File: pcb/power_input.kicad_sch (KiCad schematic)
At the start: 16 parts, among them K1 G4A-1A-E DC12, Q1 AO3400A

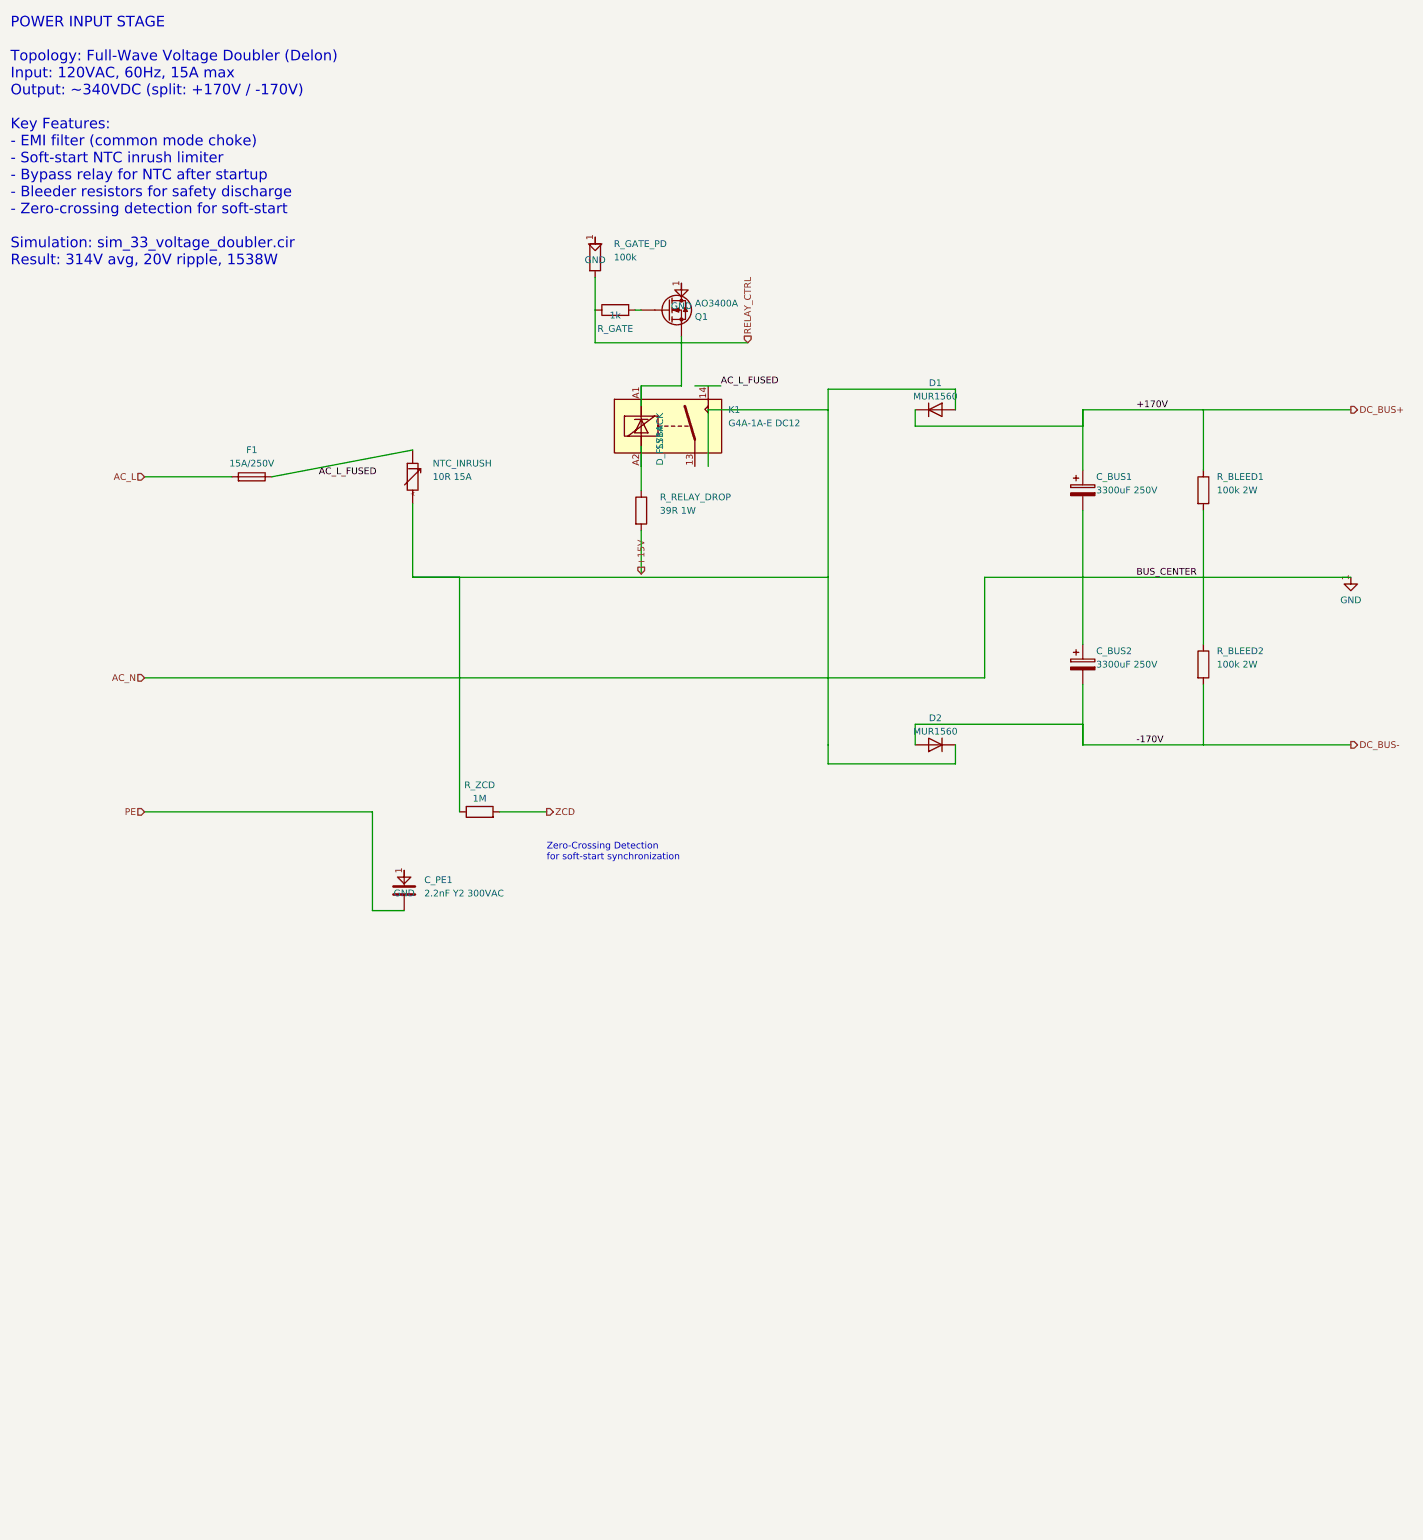
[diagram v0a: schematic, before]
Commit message: feat: generate KiCad schematics from atopile netlist
scripts/gen_schematics.py generates all 7 hierarchical KiCad schematic
files (root + 6 sub-sheets) from elec/build/default.net:

- Synthesizes box symbols from netlist libpart pin counts
- Pure label-per-pin connectivity (no wires)
- Hierarchical labels for inter-sheet nets
- Deterministic UUIDs from atopile tstamps
- Built-in oracle verifies connectivity partition isomorphism
- No-connect markers on intentionally-unconnected pins

Oracle: ORACLE PASS — 346 pin assignments, 73 multi-node nets,
connectivity partitions isomorphic.

Integrated into Makefile via 'make schematics' target.
Manifest entry added per repo convention.
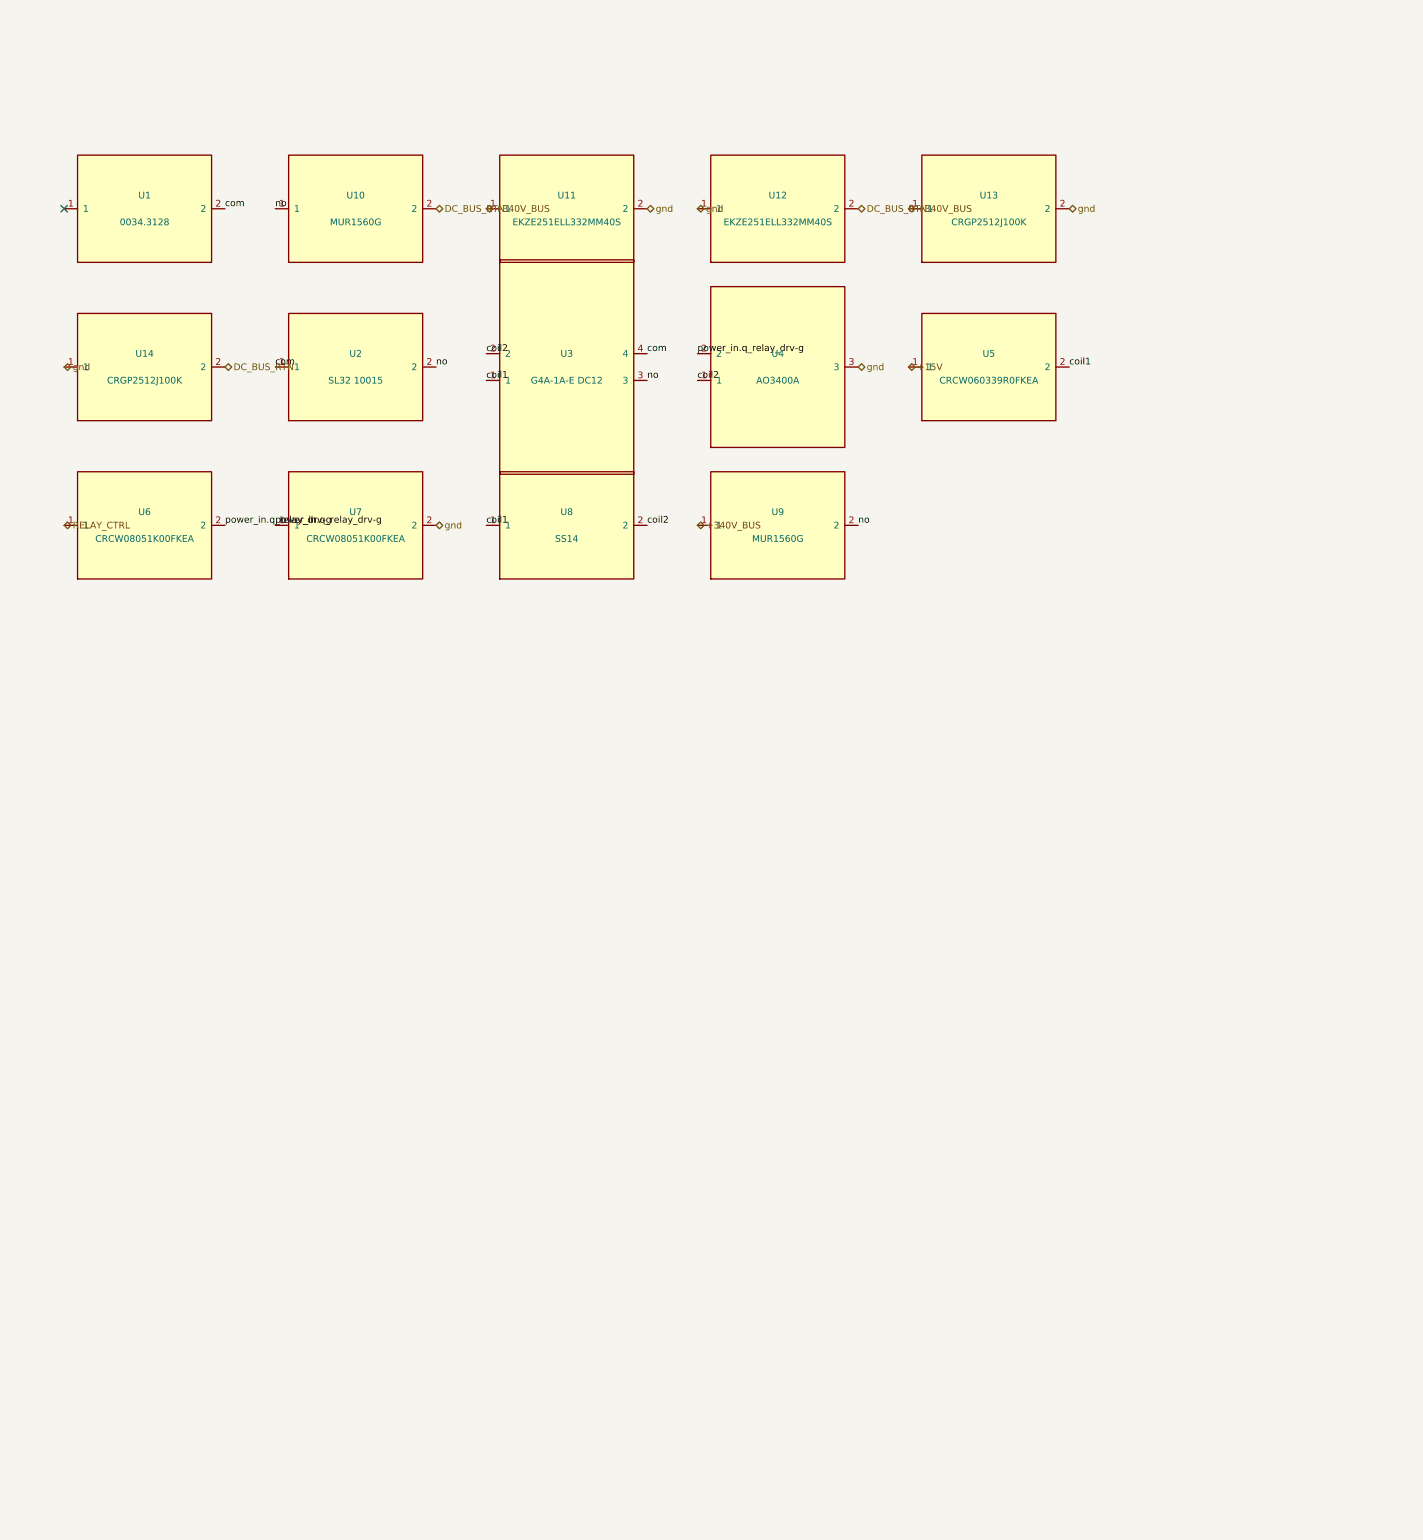
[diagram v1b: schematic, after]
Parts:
- removed C_BUS1, C_BUS2: 3300uF 250V, Capacitor_THT:CP_Radial_D35.0mm_P10.00mm_SnapIn, symbol Device:C_Polarized
- removed C_PE1: 2.2nF Y2 300VAC, Capacitor_THT:C_Disc_D10.5mm_W5.0mm_P7.50mm, symbol Device:C
- removed D1, D2: MUR1560, Package_TO_SOT_THT:TO-220-2_Vertical, symbol Device:D
- removed D_FLYBACK: SS14, Diode_SMD:D_SMA, symbol Device:D
- removed F1: 15A/250V, Fuse:Fuse_Holder_5x20mm, symbol Device:Fuse
- removed K1: G4A-1A-E DC12, temper:Relay_SPST_Omron-G4A-E, symbol Relay:Relay_SPST-NO
- removed NTC_INRUSH: 10R 15A, Resistor_THT:R_Disc_D15.0mm_W7.0mm_P7.5mm, symbol Device:Thermistor_NTC
- removed Q1: AO3400A, Package_TO_SOT_SMD:SOT-23, symbol Device:Q_NMOS
- removed R_BLEED1, R_BLEED2: 100k 2W, Resistor_SMD:R_2512_6332Metric, symbol Device:R
- removed R_GATE: 1k, Resistor_SMD:R_0805_2012Metric, symbol Device:R
- removed R_GATE_PD: 100k, Resistor_SMD:R_0805_2012Metric, symbol Device:R
- removed R_RELAY_DROP: 39R 1W, Resistor_THT:R_Axial_DIN0207_L6.3mm_D2.5mm_P10.16mm_Horizontal, symbol Device:R
- removed R_ZCD: 1M, Resistor_SMD:R_1206_3216Metric, symbol Device:R
- added U1: 0034.3128, Fuse:Fuse_Holder_5x20mm, symbol 0034.3128
- added U10, U9: MUR1560G, Package_TO_SOT_THT:TO-220-2_Vertical, symbol MUR1560G
- added U11, U12: EKZE251ELL332MM40S, Capacitor_THT:CP_Radial_D35.0mm_P10.00mm_SnapIn, symbol EKZE251ELL332MM40S
- added U13, U14: CRGP2512J100K, Resistor_SMD:R_2512_6332Metric, symbol CRGP2512J100K
- added U2: SL32 10015, Resistor_THT:R_Disc_D15.0mm_W7.0mm_P7.5mm, symbol SL32_10015
- added U3: G4A-1A-E DC12, temper:Relay_SPST_Omron-G4A-E, symbol G4A-1A-E_DC12
- added U4: AO3400A, Package_TO_SOT_SMD:SOT-23, symbol AO3400A
- added U5: CRCW060339R0FKEA, Resistor_THT:R_Axial_DIN0207_L6.3mm_D2.5mm_P10.16mm_Horizontal, symbol CRCW060339R0FKEA
- added U6, U7: CRCW08051K00FKEA, Resistor_SMD:R_0805_2012Metric, symbol CRCW08051K00FKEA
- added U8: SS14, Diode_SMD:D_SMA, symbol SS14
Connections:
- net +15V: now also U5.1
- net RELAY_CTRL: now also U6.1
- new net +340V_BUS: U11.1, U13.1, U9.1
- new net DC_BUS_RTN: U10.2, U12.2, U14.2
- new net coil1: U3.1, U5.2, U8.1
- new net coil2: U3.2, U4.1, U8.2
- new net com: U1.2, U2.1, U3.4
- new net gnd: U11.2, U12.1, U13.2, U14.1, U4.3, U7.2
- new net no: U10.1, U2.2, U3.3, U9.2
- new net power_in.q_relay_drv-g: U4.2, U6.2, U7.1
- no-connect marks 0 -> 1
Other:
- note removed: "POWER INPUT STAGE Topology: Full-Wave Voltage Doubler (Delon) Input: 120VAC, 60Hz, 15A max Output: ~340VDC (split: +170V / -170V) Key Features: - EMI filter (common mode choke) - Soft-start NTC inrush limiter - Bypass relay for NTC after startup - Bleeder resistors for safety discharge - Zero-crossing detection for soft-start Simulation: sim_33_voltage_doubler.cir Result: 314V avg, 20V ripple, 15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"
- note removed: "Zero-Crossing Detection for soft-start synchronization"
- title: Power Input Stage -> Power_Input

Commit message: chore: regenerate schematics from atopile netlist (#228)
Generated from elec/build/default.net via gen_schematics.py.
Adds 23 new components from discharge (17), aux_supply (4), and
thermal (2) modules that were previously un-mapped and absent.
Root sheet layout re-stacked with dynamic spacing.
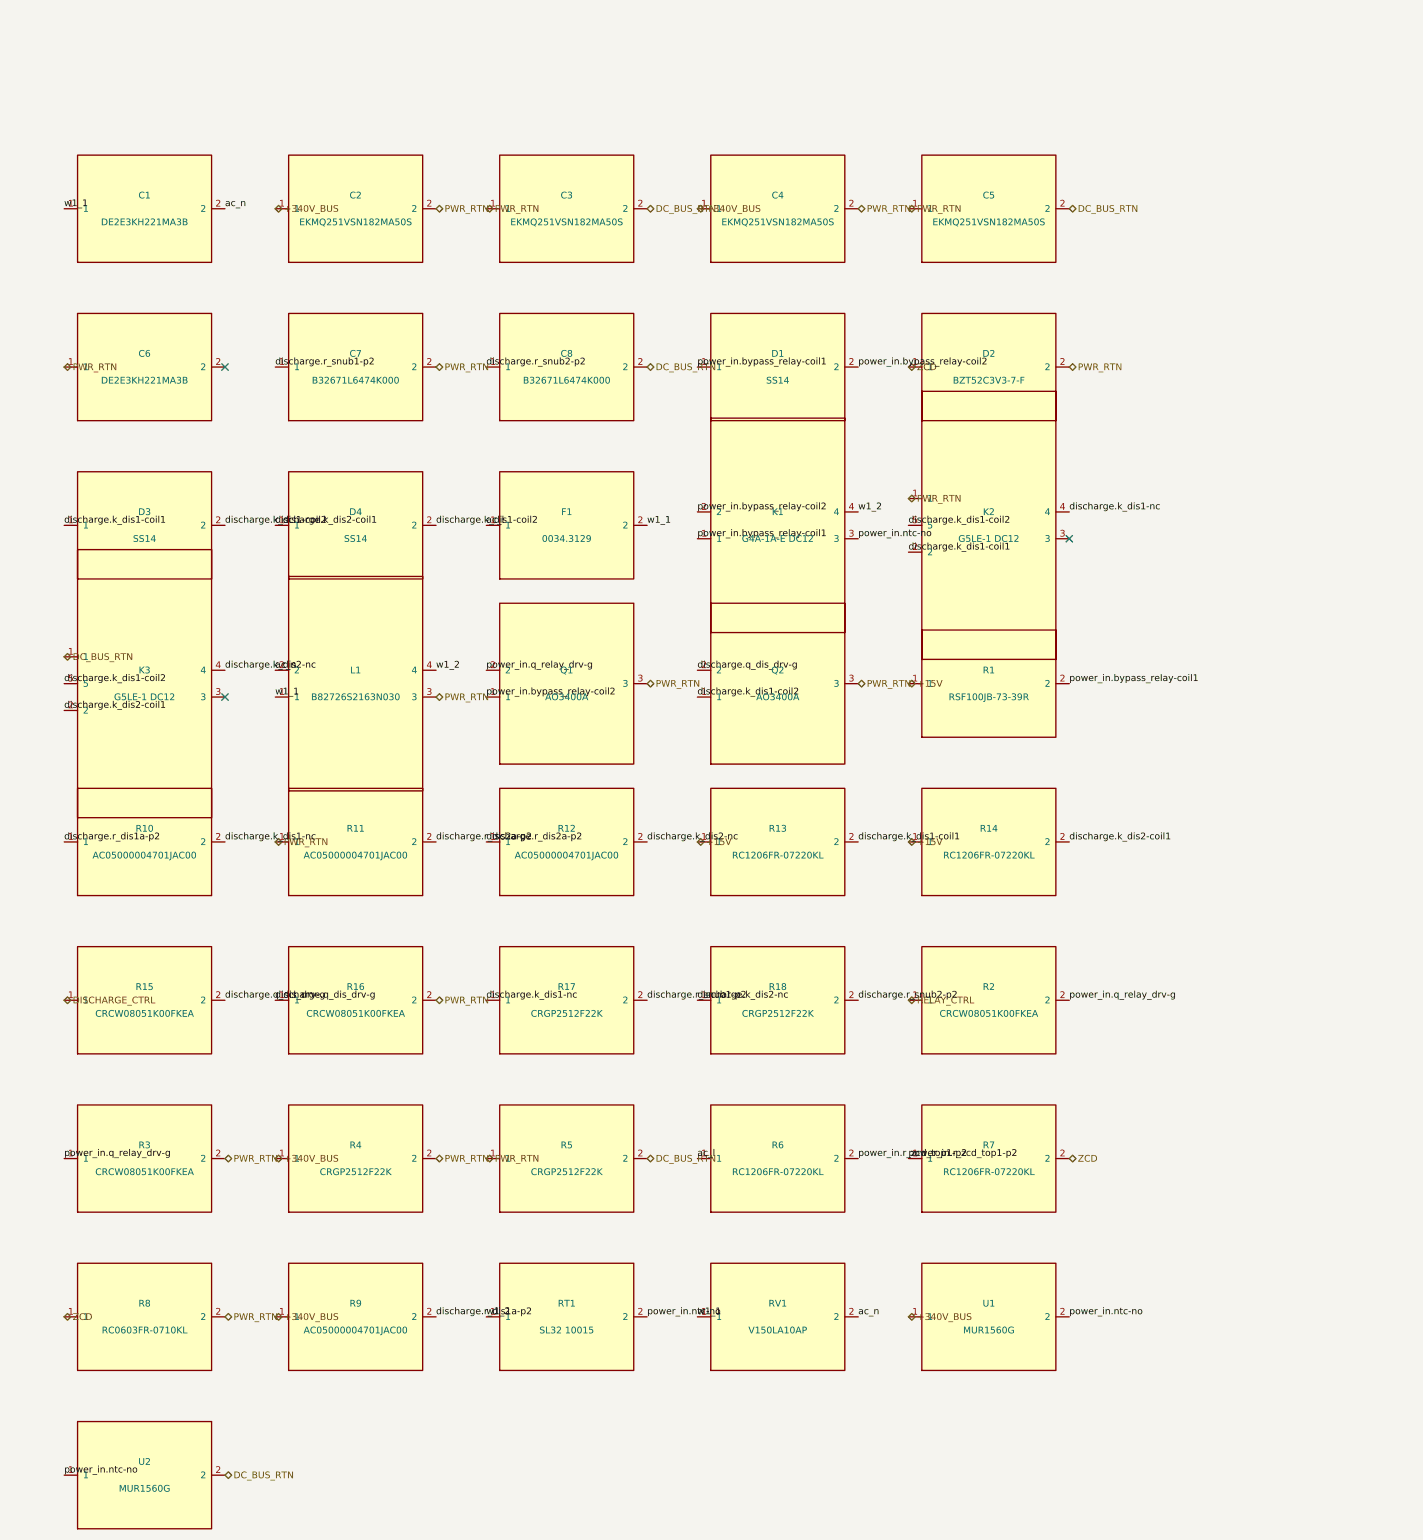
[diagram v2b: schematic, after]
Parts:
- added C1, C6: DE2E3KH221MA3B, Capacitor_THT:C_Disc_D10.0mm_W5.0mm_P5.00mm, symbol DE2E3KH221MA3B
- added C4, C5: EKMQ251VSN182MA50S, Capacitor_THT:CP_Radial_D35.0mm_P10.00mm_SnapIn, symbol EKMQ251VSN182MA50S
- added C7, C8: B32671L6474K000, Capacitor_THT:C_Rect_L18.0mm_W11.0mm_P15.00mm_FKS3_FKP3, symbol B32671L6474K000
- added D2: BZT52C3V3-7-F, Diode_SMD:D_SOD-123, symbol BZT52C3V3-7-F
- added D3, D4: SS14, Diode_SMD:D_SMA, symbol SS14
- added K2, K3: G5LE-1 DC12, Relay_THT:Relay_SPDT_Omron-G5LE-1, symbol G5LE-1_DC12
- added L1: B82726S2163N030, temper:CMC_B82726S, symbol B82726S2163N030
- added Q2: AO3400A, Package_TO_SOT_SMD:SOT-23, symbol AO3400A
- added R10, R11, R12, R9: AC05000004701JAC00, Resistor_THT:R_Axial_DIN0918_L18.0mm_D9.0mm_P22.86mm_Horizontal, symbol AC05000004701JAC00
- added R13, R14, R6, R7: RC1206FR-07220KL, Resistor_SMD:R_1206_3216Metric, symbol RC1206FR-07220KL
- added R15, R16: CRCW08051K00FKEA, Resistor_SMD:R_0805_2012Metric, symbol CRCW08051K00FKEA
- added R17, R18: CRGP2512F22K, Resistor_SMD:R_2512_6332Metric, symbol CRGP2512F22K
- added R8: RC0603FR-0710KL, Resistor_SMD:R_0603_1608Metric, symbol RC0603FR-0710KL
- added RV1: V150LA10AP, Varistor:RV_Disc_D15.5mm_W5.2mm_P7.5mm, symbol V150LA10AP
- C2: renamed from U11; value EKZE251ELL332MM40S -> EKMQ251VSN182MA50S; symbol EKZE251ELL332MM40S -> EKMQ251VSN182MA50S
- C3: renamed from U12; value EKZE251ELL332MM40S -> EKMQ251VSN182MA50S; symbol EKZE251ELL332MM40S -> EKMQ251VSN182MA50S
- F1: renamed from U1; value 0034.3128 -> 0034.3129; symbol 0034.3128 -> 0034.3129
- R1: renamed from U5; value CRCW060339R0FKEA -> RSF100JB-73-39R; symbol CRCW060339R0FKEA -> RSF100JB-73-39R
- R4: renamed from U13; value CRGP2512J100K -> CRGP2512F22K; symbol CRGP2512J100K -> CRGP2512F22K
- R5: renamed from U14; value CRGP2512J100K -> CRGP2512F22K; symbol CRGP2512J100K -> CRGP2512F22K
- renumbered U8 to D1, U3 to K1, U4 to Q1, U6 to R2, U7 to R3, U2 to RT1, U9 to U1, U10 to U2
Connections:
- net +15V: now also R13.1, R14.1
- net +340V_BUS: now also C4.1, R9.1
- net DC_BUS_RTN: now also C5.2, C8.2, K3.1
- net ac_l: now reaches F1.1
- net ac_l: now also R6.1
- net coil1 renamed power_in.bypass_relay-coil1
- net coil2 renamed power_in.bypass_relay-coil2
- net com renamed w1_2
- net w1_2: now also L1.4; no longer F1.2
- net gnd renamed PWR_RTN
- net PWR_RTN: now also C4.2, C5.1, C6.1, C7.2, D2.2, K2.1, L1.3, Q2.3, R11.1, R16.2, R8.2
- net no renamed power_in.ntc-no
- new net DISCHARGE_CTRL: R15.1
- new net ZCD: D2.1, R7.2, R8.1
- new net ac_n: C1.2, L1.2, RV1.2
- new net discharge.k_dis1-coil1: D3.1, K2.2, R13.2
- new net discharge.k_dis1-coil2: D3.2, D4.2, K2.5, K3.5, Q2.1
- new net discharge.k_dis1-nc: K2.4, R10.2, R17.1
- new net discharge.k_dis2-coil1: D4.1, K3.2, R14.2
- new net discharge.k_dis2-nc: K3.4, R12.2, R18.1
- new net discharge.q_dis_drv-g: Q2.2, R15.2, R16.1
- new net discharge.r_dis1a-p2: R10.1, R9.2
- new net discharge.r_dis2a-p2: R11.2, R12.1
- new net discharge.r_snub1-p2: C7.1, R17.2
- new net discharge.r_snub2-p2: C8.1, R18.2
- new net power_in.r_zcd_top1-p2: R6.2, R7.1
- new net w1_1: C1.1, F1.2, L1.1, RV1.1
- no-connect marks 1 -> 3
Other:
- moved on the sheet: C2, C3, D1, F1, K1, Q1, R1, R2, R3, R4, R5, RT1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
